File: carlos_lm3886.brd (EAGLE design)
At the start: 48.3 x 48.3 mm, 19 parts

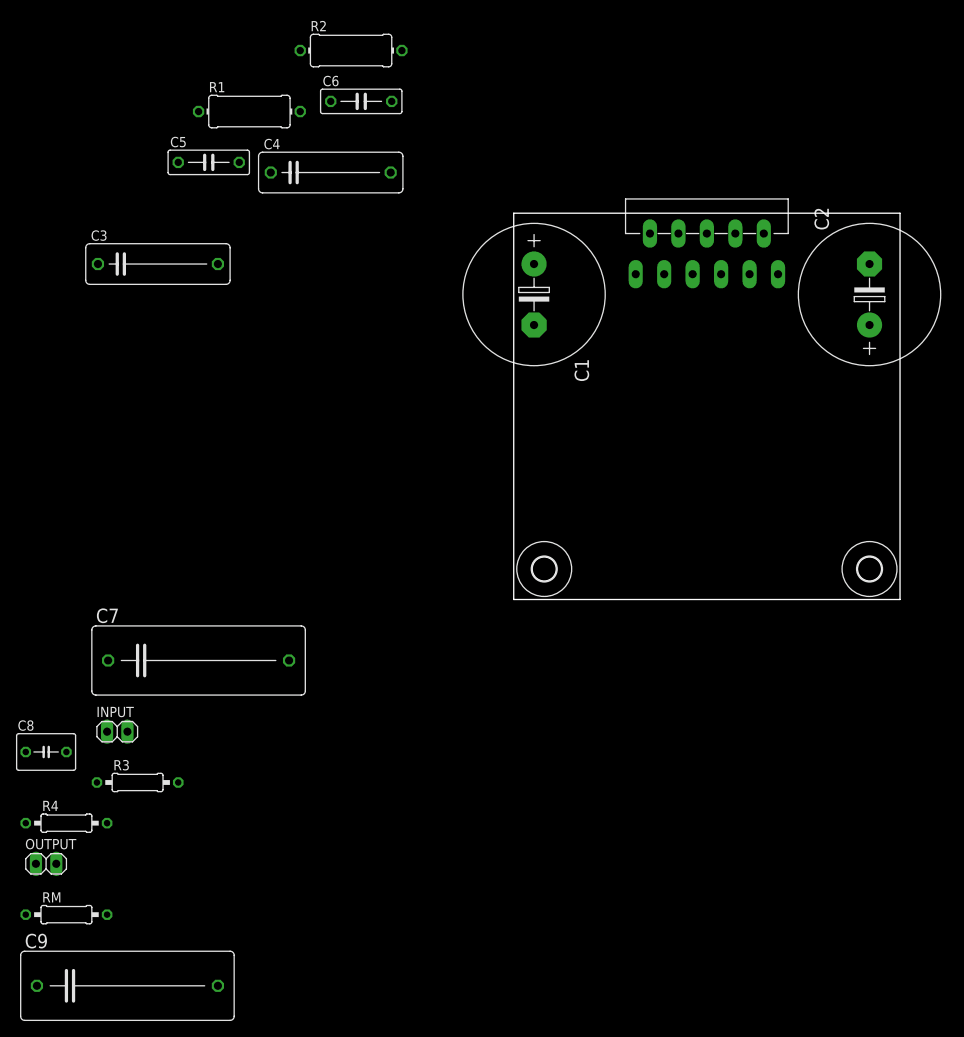
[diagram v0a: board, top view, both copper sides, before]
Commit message: layout without traces completed
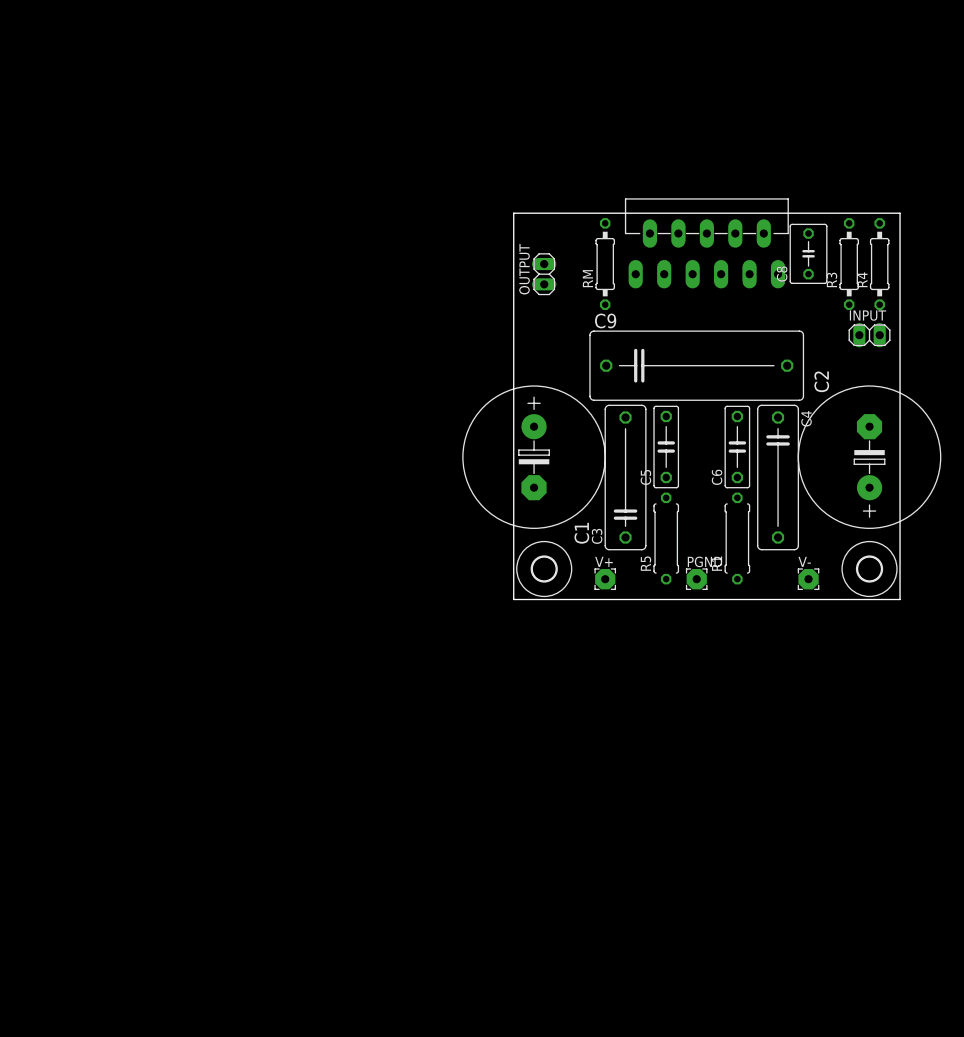
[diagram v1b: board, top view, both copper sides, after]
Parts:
- removed C7: 2.2uF, rcl:C225-087X268
- removed R2: 0.1R 1W, rcl:0411/12
- added PGND, V+, V-: (no value), wirepad:2,54/1,0
- added R5: 0.1R 1W, resistor:0309/10
- R1: device rcl:0411/12 -> resistor:0309/10
- moved R4 123.3 mm to (45.7, 41.9), turned to 90 degrees
- moved C8 113.8 mm to (36.8, 43.2), turned to 90 degrees
- moved R3 110.0 mm to (41.9, 41.9), turned to 90 degrees
- moved INPUT 106.2 mm to (44.5, 33.0)
- moved RM 105.5 mm to (11.4, 41.9), turned to 90 degrees
- moved C9 105.2 mm to (22.9, 29.2)
- moved OUTPUT 96.4 mm to (3.81, 40.6), turned to 90 degrees
- moved R1 81.0 mm to (27.9, 7.62), turned to 90 degrees
- moved C4 67.6 mm to (33.0, 15.2), turned to 270 degrees
- moved C5 67.3 mm to (19.1, 19.1), turned to 90 degrees
- moved C3 64.2 mm to (14.0, 15.2), turned to 90 degrees
- moved C6 63.8 mm to (27.9, 19.1), turned to 90 degrees
- moved C1 20.3 mm to (2.54, 17.8)
- moved C2 20.3 mm to (44.5, 17.8)
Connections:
- removed net N$2: C7.2, R3.1
- net GND: now also PGND.1
- net N$1: now also R3.1; no longer C7.1
- net N$3: now also R1.2; no longer R2.1
- net N$4: now also R5.1; no longer R1.2
- net V+: now also R5.2, V+.1; no longer R1.1
- net V-: now also R1.1, V-.1; no longer R2.2

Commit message: final?
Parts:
- removed OUTPUT: (no value), pinhead:1X02
- removed RM: 10k, rcl:0207/10
- added A1, A2, CHASSIS, OUT+, OUT-: (no value), wirepad:2,54/1,0
- added U$4: (no value), holes:3,0
- moved C9 24.2 mm to (24.1, 5.08)
- moved R5 20.5 mm to (21.6, 27.9)
- moved R1 20.3 mm to (27.9, 27.9), turned to 270 degrees
- moved PGND 14.1 mm to (24.8, 16.5)
- moved INPUT 11.5 mm to (45.7, 44.5), turned to 315 degrees
- moved R4 8.52 mm to (38.1, 38.1), turned to 180 degrees
- moved C3 8.03 mm to (16.5, 22.9)
- moved C4 7.62 mm to (33.0, 22.9)
- moved V+ 6.84 mm to (8.89, 8.89)
- moved V- 6.84 mm to (39.4, 8.89)
- moved C1 3.59 mm to (5.08, 20.3), turned to 290 degrees
- moved C5 3.59 mm to (21.6, 16.5)
- moved R3 2.54 mm to (44.5, 41.9), turned to 135 degrees
- moved C2 2.54 mm to (44.5, 20.3), turned to 70 degrees
- moved C6 2.54 mm to (27.9, 16.5), turned to 270 degrees
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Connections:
- removed net N$8: RM.2, U$1.8
- net GND: now also A1.1, A2.1, CHASSIS.1, OUT-.1; no longer OUTPUT.2
- net N$7: now also OUT+.1; no longer OUTPUT.1
- net V-: no longer RM.1
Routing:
- net GND: track 0.00 -> 132.7 mm
- net V-: track 0.00 -> 60.9 mm
- net V+: track 0.00 -> 59.1 mm
- net N$6: track 0.00 -> 12.0 mm
- net N$5: track 0.00 -> 9.62 mm
- net N$7: track 0.00 -> 8.50 mm
- net N$1: track 0.00 -> 5.42 mm
- net N$4: track 0.00 -> 2.54 mm
- net N$3: track 0.00 -> 2.54 mm
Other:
- board size 48.3 x 48.3 mm -> 49.5 x 48.3 mm
